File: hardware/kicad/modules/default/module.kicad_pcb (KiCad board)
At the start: 4 copper layers, 12.7 x 11.6 mm, 42 parts, among them J1 MOD_CONN, J10 MOD_CONN, J11 MOD_CONN, J12 MOD_CONN, J13 MOD_CONN, J14 MOD_CONN, J15 MOD_CONN, J16 MOD_CONN, J17 MOD_CONN, J18 MOD_CONN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

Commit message: change tvs diode fix module and calc
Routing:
- net +3V3: track 7.11 -> 22.3 mm
- net GND: track 2.16 -> 12.0 mm
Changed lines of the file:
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@@
+	)
+	(segment
+		(start 153.5707 92.7307)
+		(end 153 92.16)
+		(width 0.5)
+		(layer "In2.Cu")
+		(net 1)
+	)
+	(segment
+		(start 156.35 92.7307)
+		(end 153.5707 92.7307)
+		(width 0.5)
+		(layer "In2.Cu")
+		(net 1)
+	)
+	(segment
+		(start 156.015 98.829999)
+		(end 156.35 98.494999)
+		(width 0.5)
+		(layer "B.Cu")
+		(net 1)
+	)
+	(segment
+		(start 156.35 98.494999)
+		(end 156.35 92.7307)
+		(width 0.5)
+		(layer "B.Cu")
+		(net 1)
 	)
 	(segment
@@
 	)
 	(segment
+		(start 145.075 88.869999)
+		(end 145.700001 88.869999)
+		(width 0.5)
+		(layer "In1.Cu")
+		(net 3)
+	)
+	(segment
+		(start 154.48 89.54)
+		(end 154.51 89.54)
+		(width 0.5)
+		(layer "In1.Cu")
+		(net 3)
+	)
+	(segment
 		(start 153.825 94.01)
 		(end 151.975 92.16)
@@
 	)
 	(segment
+		(start 153.49 88.55)
+		(end 154.48 89.54)
+		(width 0.5)
+		(layer "In1.Cu")
+		(net 3)
+	)
+	(segment
+		(start 145.700001 88.869999)
+		(end 146.02 88.55)
+		(width 0.5)
+		(layer "In1.Cu")
+		(net 3)
+	)
+	(segment
+		(start 154.51 89.54)
+		(end 154.51 90.62)
+		(width 0.5)
+		(layer "In1.Cu")
+		(net 3)
+	)
+	(segment
 		(start 153.825 95.76)
 		(end 153.825 94.01)
 		(width 0.25)
+		(layer "In1.Cu")
+		(net 3)
+	)
+	(segment
+		(start 152.16 91)
+		(end 151 92.16)
+		(width 0.5)
+		(layer "In1.Cu")
+		(net 3)
+	)
+	(segment
+		(start 146.02 88.55)
+		(end 153.49 88.55)
+		(width 0.5)
+		(layer "In1.Cu")
+		(net 3)
+	)
+	(segment
+		(start 154.51 90.62)
+		(end 154.13 91)
+		(width 0.5)
+		(layer "In1.Cu")
+		(net 3)
+	)
+	(segment
+		(start 154.13 91)
+		(end 152.16 91)
+		(width 0.5)
 		(layer "In1.Cu")
 		(net 3)
@@
 	)
 	(zone
+		(net 3)
+		(net_name "+3V3")
+		(layer "In1.Cu")
+		(name "$teardrop_padvia$")
+		(hatch full 0.1)
+		(priority 30000)
+		(attr
+			(teardrop
+				(type padvia)
+			)
+		)
+		(connect_pads yes
+			(clearance 0)
+		)
+		(min_thickness 0.0254)
+		(filled_areas_thickness no)
+		(fill yes
+			(thermal_gap 0.5)
+			(thermal_bridge_width 0.5)
+			(island_removal_mode 1)
+			(island_area_min 10)
+		)
+		(polygon
+			(pts
+				(xy 151.530329 91.276117) (xy 151.378852 91.418137) (xy 151.259834 91.506255) (xy 151.144389 91.565556)
+				(xy 151.003626 91.621128) (xy 150.808658 91.69806) (xy 150.999293 92.160707) (xy 151.46194 92.351342)
+				(xy 151.538871 92.156373) (xy 151.594443 92.01561) (xy 151.653744 91.900164) (xy 151.741861 91.781147)
+				(xy 151.883883 91.629671)
+			)
+		)
+	)
+	(zone
 		(net 17)
 		(net_name "MOD_ExB5")
@@
 	)
 	(zone
+		(net 1)
+		(net_name "GND")
+		(layer "In2.Cu")
+		(name "$teardrop_padvia$")
+		(hatch full 0.1)
+		(priority 30001)
+		(attr
+			(teardrop
+				(type padvia)
+			)
+		)
+		(connect_pads yes
+			(clearance 0)
+		)
+		(min_thickness 0.0254)
+		(filled_areas_thickness no)
+		(fill yes
+			(thermal_gap 0.5)
+			(thermal_bridge_width 0.5)
+			(island_removal_mode 1)
+			(island_area_min 10)
+		)
+		(polygon
+			(pts
+				(xy 155.4356 92.9807) (xy 155.52704 92.997276) (xy 155.61848 93.026284) (xy 155.70992 93.067723)
+				(xy 155.80136 93.121595) (xy 155.8928 93.1879) (xy 156.351 92.7307) (xy 155.8928 92.2735) (xy 155.80136 92.339804)
+				(xy 155.70992 92.393676) (xy 155.61848 92.435115) (xy 155.52704 92.464123) (xy 155.4356 92.4807)
+			)
+		)
+	)
+	(zone
 		(net 14)
 		(net_name "MOD_ExB2")
@@
 	)
 	(zone
+		(net 1)
+		(net_name "GND")
+		(layer "In2.Cu")
+		(name "$teardrop_padvia$")
+		(hatch full 0.1)
+		(priority 30000)
+		(attr
+			(teardrop
+				(type padvia)
+			)
+		)
+		(connect_pads yes
+			(clearance 0)
+		)
+		(min_thickness 0.0254)
+		(filled_areas_thickness no)
+		(fill yes
+			(thermal_gap 0.5)
+			(thermal_bridge_width 0.5)
+			(island_removal_mode 1)
+			(island_area_min 10)
+		)
+		(polygon
+			(pts
+				(xy 153.763608 92.4807) (xy 153.629045 92.453802) (xy 153.561802 92.379525) (xy 153.531672 92.267493)
+				(xy 153.508453 92.127329) (xy 153.46194 91.968658) (xy 152.999 92.16) (xy 152.808658 92.62194) (xy 153.03996 92.734204)
+				(xy 153.201475 92.832546) (xy 153.342835 92.910631) (xy 153.513669 92.962127) (xy 153.763608 92.9807)
+			)
+		)
+	)
+	(zone
 		(net 16)
 		(net_name "MOD_ExB4")
@@
 			)
 		)
+	)
+	(zone
+		(net 1)
+		(net_name "GND")
+		(layer "B.Cu")
+		(name "$teardrop_padvia$")
+		(hatch full 0.1)
+		(priority 30000)
+		(attr
+			(teardrop
+				(type padvia)
+			)
+		)
+		(connect_pads yes
+			(clearance 0)
+		)
+		(min_thickness 0.0254)
+		(filled_areas_thickness no)
+		(fill yes
+			(thermal_gap 0.5)
+			(thermal_bridge_width 0.5)
+			(island_removal_mode 1)
+			(island_area_min 10)
+		)
+		(polygon
+			(pts
+				(xy 156.6 93.6451) (xy 156.64144 93.528796) (xy 156.68288 93.424924) (xy 156.724319 93.333484) (xy 156.765759 93.254476)
+				(xy 156.8072 93.1879) (xy 156.35 92.7297) (xy 155.8928 93.1879) (xy 155.93424 93.254476) (xy 155.97568 93.333484)
+				(xy 156.017119 93.424923) (xy 156.058559 93.528796) (xy 156.1 93.6451)
+			)
+		)

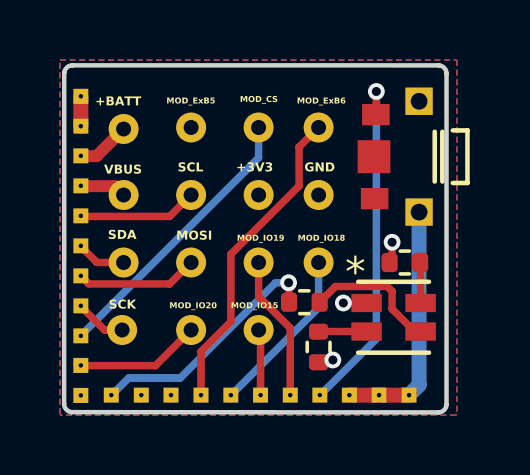
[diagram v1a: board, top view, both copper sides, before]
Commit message: improve module silkscreen
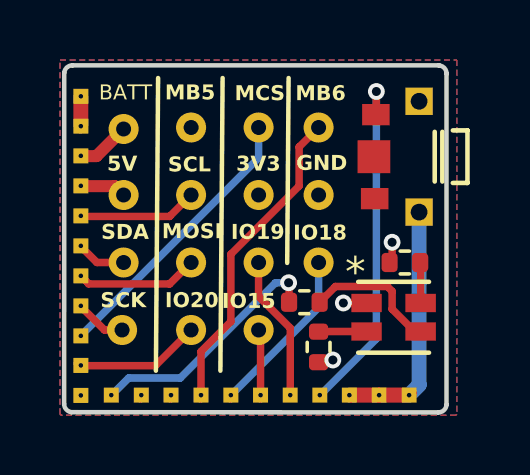
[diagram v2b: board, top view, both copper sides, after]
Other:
- board text added: "3V3"
- board text added: "5V"
- board text added: "BATT"
- board text added: "IO15"
- board text added: "IO18"
- board text added: "IO19"
- board text added: "IO20"
- board text added: "MB5"
- board text added: "MB6"
- board text added: "MCS"
- board text removed: "+3V3"
- board text removed: "+BATT"
- board text removed: "MOD_CS"
- board text removed: "MOD_ExB5"
- board text removed: "MOD_ExB6"
- board text removed: "MOD_IO15"
- board text removed: "MOD_IO18"
- board text removed: "MOD_IO19"
- board text removed: "MOD_IO20"
- board text removed: "VBUS"

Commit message: add new module
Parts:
- removed R1, R2, R3: 330, Yatchy:R_0402_1005Metric
- added D1: LED, LED_SMD:LED_0402_1005Metric, B.Cu at (156.7, 94.8)
- added RN1: 330 ohm, Yatchy:R_Array_Concave_4x0402, F.Cu at (152.8, 97.1)
- turned TP14 to 0 degrees
- turned LED1 to 90 degrees
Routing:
- net MOD_ExB4: track 7.39 -> 17.7 mm
- net MOD_ExB3: track 8.12 -> 16.9 mm
- net Net-(D1-K): track 0.00 -> 6.28 mm, vias 0 -> 1
- net GND: track 12.0 -> 5.74 mm
- net MOD_ExB2: track 13.2 -> 8.67 mm, vias 1 -> 0
- net MOD_ExB5: track 9.95 -> 14.1 mm
- net +3V3: track 22.3 -> 25.0 mm, vias 1 -> 2
- net Net-(RN1-R2.2): track 1.36 -> 3.17 mm
- net BTN_4: track 11.7 -> 13.5 mm
- net Net-(RN1-R4.2): track 1.60 -> 2.96 mm
- net MOD_ExB6: track 10.6 -> 11.4 mm
- net Net-(RN1-R3.2): track 4.55 -> 3.79 mm
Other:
- board text added: "LED"
- board text removed: "MB5"
